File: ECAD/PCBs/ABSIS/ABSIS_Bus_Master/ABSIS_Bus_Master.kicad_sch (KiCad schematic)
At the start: 57 parts, among them IC1 THVD1410DR, IC2 THVD1410DR, IC3 THVD1410DR, J1 Mini-Fit Jr. 2x04, J2 Mini-Fit Jr. 2x03, J3 Mini-Fit Jr. 2x03, J4 Mini-Fit Jr. 2x03, J5 PinHeader_2x11, J6 Screw_Terminal_01x01, P1 Power, P2 Analog, P3 Analog, P4 Digital, P5 PWM, P6 PWM, P7 Communication

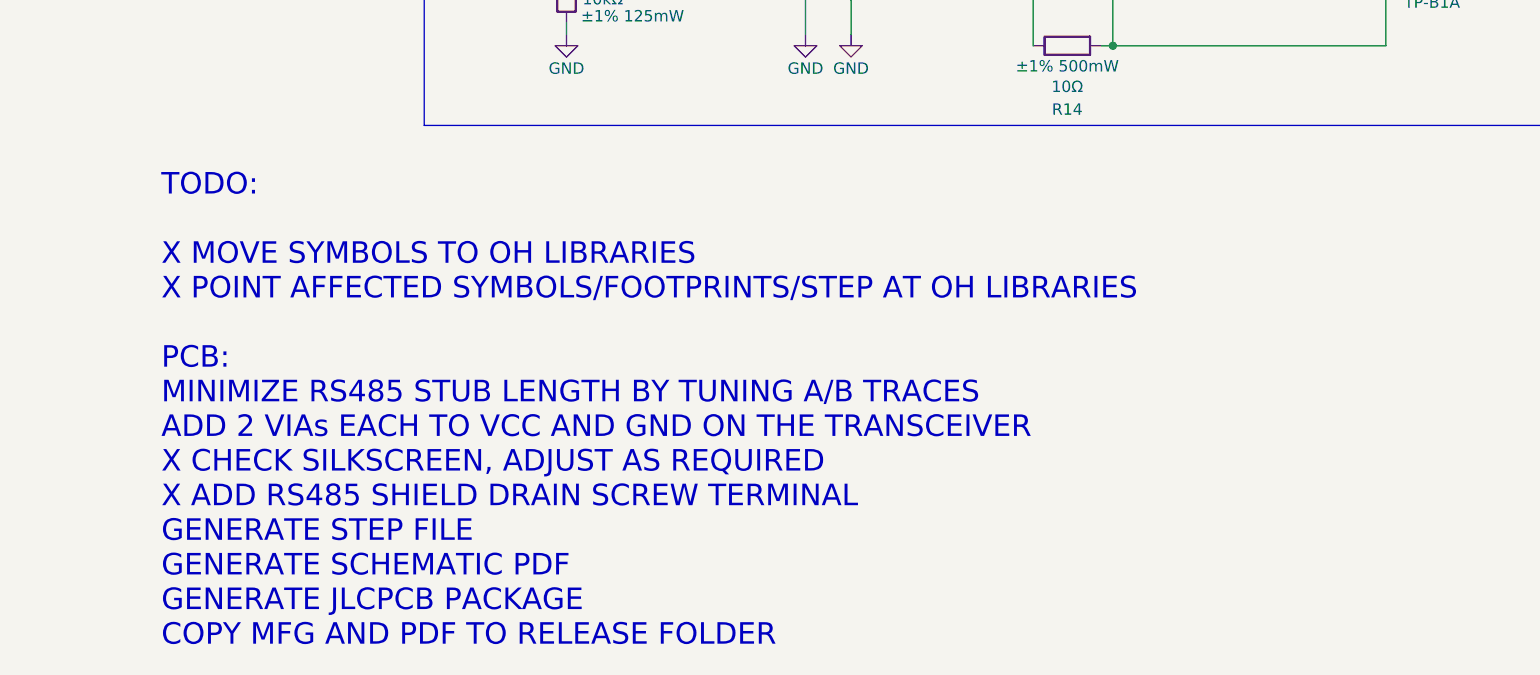
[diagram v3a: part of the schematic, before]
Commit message: Finished ASBSIS Bus Master Updates
Updated A/B track lengths for Bus 1 and 2
Generated manufacturing files, step, and PDF of schematic
Copied manufacturing files and PDF to release folder
Added `JLCJLCJLCJLC` silkscreen for JLC order number replacement during fab.
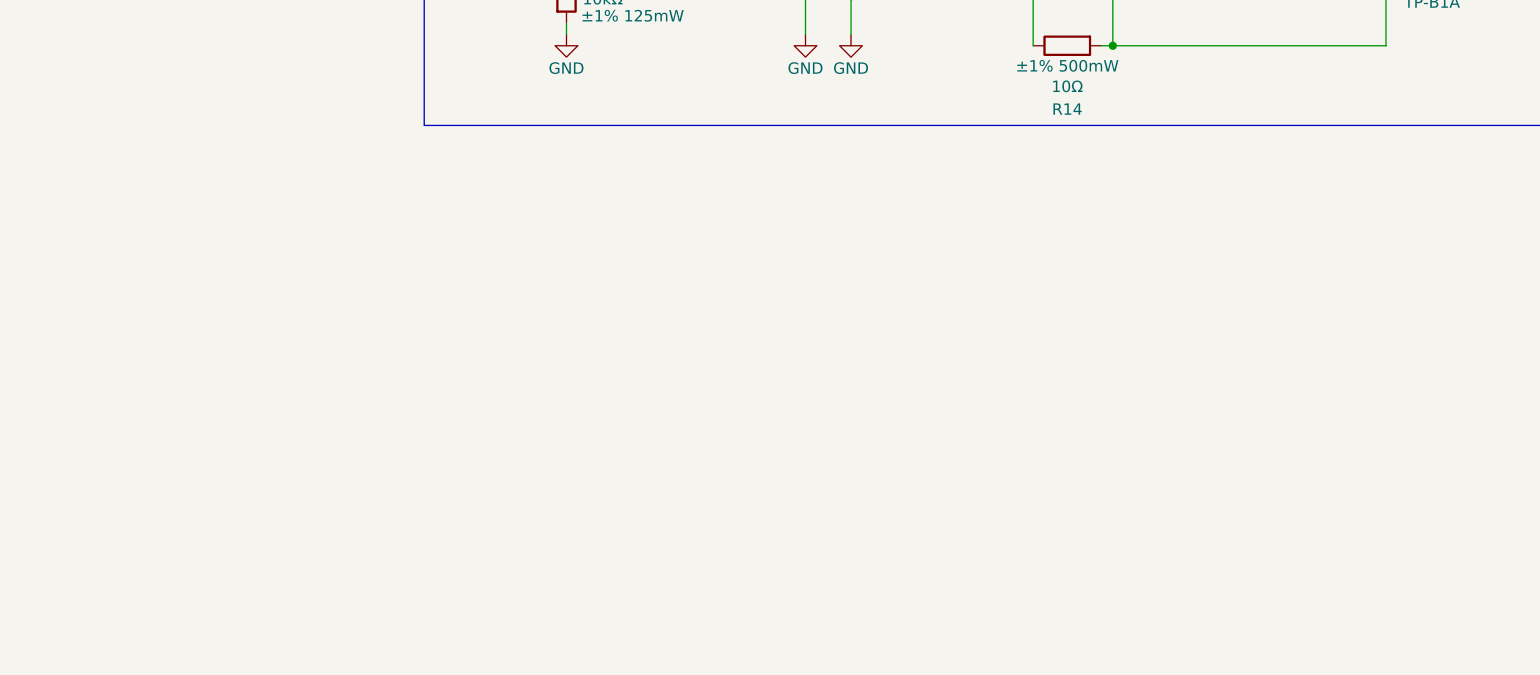
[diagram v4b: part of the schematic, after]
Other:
- note removed: "TODO: X MOVE SYMBOLS TO OH LIBRARIES X POINT AFFECTED SYMBOLS/FOOTPRINTS/STEP AT OH LIBRARIES PCB: MINIMIZE RS485 STUB LENGTH BY TUNING A/B TRACES ADD 2 VIAs EACH TO VCC AND GND ON THE TRANSCEIVER X CHECK SILKSCREEN, ADJUST AS REQUIRED X ADD RS485 SHIELD DRAIN SCREW TERMINAL GENERATE STEP FILE GENERATE SCHEMATIC PDF GENERATE JLCPCB PACKAGE COPY MFG AND PDF TO RELEASE FOLDER"
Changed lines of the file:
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@@
-		)
-	)
-	(text "TODO:\n\nX MOVE SYMBOLS TO OH LIBRARIES\nX POINT AFFECTED SYMBOLS/FOOTPRINTS/STEP AT OH LIBRARIES\n\nPCB:\nMINIMIZE RS485 STUB LENGTH BY TUNING A/B TRACES\nADD 2 VIAs EACH TO VCC AND GND ON THE TRANSCEIVER\nX CHECK SILKSCREEN, ADJUST AS REQUIRED\nX ADD RS485 SHIELD DRAIN SCREW TERMINAL\nGENERATE STEP FILE\nGENERATE SCHEMATIC PDF\nGENERATE JLCPCB PACKAGE\nCOPY MFG AND PDF TO RELEASE FOLDER"
-		(exclude_from_sim no)
-		(at 147.828 193.294 0)
-		(effects
-			(font
-				(size 2.4 2.4)
-			)
-			(justify left top)
 		)
 	)

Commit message: Updated ABSIS Bus Master
Changed PCB to 4 layer (12V Supply->GND->3.3V Supply->5V Supply) to increase power handling capabilities of PCB
Removed obsolete J5 IO connector
Cleaned up traces
Added thermal relief to all zones
Regenerated release files
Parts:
- removed J5: PinHeader_2x11, Connector_PinHeader_2.54mm:PinHeader_2x11_P2.54mm_Vertical, symbol OH_Symbols:PinHeader_2x11
- D4: value SS54 -> S3MB; footprint OH_Footprints:SS54 -> Diode_SMD:D_SMB; symbol OH Symbols:SS54 -> Device:D; Height 2.62 -> (none); LCSC C22452 -> C47524; Manufacturer PN SS54 -> S3MB; Manufacturer_Part_Number SS54 -> S3MB
- TP1: now left out of the parts list
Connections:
- net +12V_SUPPLY: now also D4.2 (A); no longer D4.1 (A)
- net at P1.8 (Pin_8): now also D4.1 (K); no longer D4.2 (K)
- no-connect marks 55 -> 66
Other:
- note added: "1) ABSIS RS485 BUS SPECIFICATION 1.1) BUS IS HALF DUPLEX: EITHER TRANSMITTING OR RECIEVING AT ANY GIVEN TIME. 1.2) PIN FUNCTION: R: DATA OUTPUT / D: DATA INPUT / DE HAS INTERNAL PULL-DOWN (DRIVER DISABLED BY DEFAULT) / RE HAS INTERNAL PULL-UP (RECIEVER DISABLED BY DEFAULT) 1.3) CIRCUIT CONTAINS OPEN, SHORT, AND IDLE BUS FAILSAFE WHICH PREVENTS THE SYSTEM FROM INTERPRETING ELECTRICAL NOISE AS VALI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"
- note removed: "1) J5 / IO CONNECTORS MAY NOT FUNCTION WITH DCS-BIOS WHILE MASTER FUNCTIONALITY IS IN USE. 2) ABSIS RS485 BUS SPECIFICATION 2.1) BUS IS HALF DUPLEX: EITHER TRANSMITTING OR RECIEVING AT ANY GIVEN TIME. 2.2) PIN FUNCTION: R: DATA OUTPUT / D: DATA INPUT / DE HAS INTERNAL PULL-DOWN (DRIVER DISABLED BY DEFAULT) / RE HAS INTERNAL PULL-UP (RECIEVER DISABLED BY DEFAULT) 2.3) CIRCUIT CONTAINS OPEN, SHORT,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"
- moved on the sheet: C1, C2, C3, D1, D2, D3, IC1, IC2, IC3, J1, J2, J3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
